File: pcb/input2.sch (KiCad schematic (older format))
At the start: 3 parts, among them U4 PCEngineExpansion

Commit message: Added clock selection
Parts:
- added C68, C78, C80, C81, C84, C85: 10u, custom_components:SM0603_Capa_libcms, symbol pcehd-rescue:C_Small-Device
- added C77, C79: 30p, custom_components:SM0603_Capa_libcms, symbol pcehd-rescue:C_Small-Device
- added C82, C83: 2.2u, custom_components:SM0603_Capa_libcms, symbol pcehd-rescue:C_Small-Device
- added R20, R21: 100k, custom_components:SM0603_Resistor_libcms, symbol ossc_board-rescue:R_Small
- added U14: PCM1862, custom_components:TSSOP-30_4.4x7.8mm_Pitch0.5mm_Handsoldering, symbol ossc_board-rescue:PCM1862
- added Y2: 24.576MHz, custom_components:ECS-3X9X, symbol ossc_board-rescue:Crystal_Small
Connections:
- net labels added: DVDD3V3, I2S_BCK, I2S_DATA, I2S_WS, SCL, SDA, SI_CLK0
- net labels removed: AudioL_O, AudioR_O
- wire segments 17 -> 47
- no-connect marks 10 -> 21

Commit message: Added FS7140 PLL, moved to level-shift '245
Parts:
- removed C77, C79: 30p, custom_components:SM0603_Capa_libcms, symbol pcehd-rescue:C_Small-Device
- removed C78, C80, C81, C84, C85: 10u, custom_components:SM0603_Capa_libcms, symbol pcehd-rescue:C_Small-Device
- removed C82, C83: 2.2u, custom_components:SM0603_Capa_libcms, symbol pcehd-rescue:C_Small-Device
- removed R20, R21: 100k, custom_components:SM0603_Resistor_libcms, symbol ossc_board-rescue:R_Small
- removed U14: PCM1862, custom_components:TSSOP-30_4.4x7.8mm_Pitch0.5mm_Handsoldering, symbol ossc_board-rescue:PCM1862
- removed Y2: 24.576MHz, custom_components:ECS-3X9X, symbol ossc_board-rescue:Crystal_Small
- added C24, C29: 0.1u, custom_components:SM0603_Capa_libcms, symbol pcehd-rescue:C_Small-Device
- added C25, C26, C30: 10u, custom_components:SM0603_Capa_libcms, symbol Device:CP_Small
- added C28, C31, C32, C78, C80: 0.1u, custom_components:SM0603_Capa_libcms, symbol pcehd-rescue:C-Device
- added C77, C79: 1u, custom_components:SM0603_Capa_libcms, symbol Device:CP_Small
- added JP1, JP2, JP3, JP4, JP5, JP6: SolderJumper_2_Open, Jumper:SolderJumper-2_P1.3mm_Open_RoundedPad1.0x1.5mm, symbol Jumper:SolderJumper_2_Open
- added R17, R19: R_Small, custom_components:SM0603_Resistor_libcms, symbol Device:R_Small
- added R20, R21: 10K, custom_components:SM0603_Resistor_libcms, symbol Device:R_Small
- added R6: 4.7k, custom_components:SM0603_Resistor_libcms, symbol pcehd-rescue:R-Device
- added U5: FS7140-01G-XTD, custom_components:FS7140-01G-XTD, symbol custom_components:FS7140-01G-XTD
- added U6: PCM1808PWR, custom_components:PCM1808PWR, symbol custom_components:PCM1808PWR
- added U7: SI5351C-B, custom_components:QFN-20-1EP_4x4mm_Pitch0.5mm_Handsoldering, symbol custom_components:Si5351C
- added U8: 74153, Package_SO:SOIC-16_3.9x9.9mm_P1.27mm, symbol 74xx_IEEE:74153
- added Y1: 25.000MHz, Crystal:Crystal_SMD_SeikoEpson_FA238-4Pin_3.2x2.5mm_HandSoldering, symbol Device:Crystal_GND24_Small
- C68: value 10u -> 0.1u
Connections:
- net labels added: AudioL, AudioR, DCK, DCKFB_I, GNDREF, HSn, IS2_BCK, IS2_DATA, IS2_WS, SI_CLK0_O, SI_CLK1_O, VCCIO
- net labels removed: DVDD3V3, SI_CLK0
- wire segments 47 -> 116
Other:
- moved on the sheet: C27, C68, D4, U4A, U4B

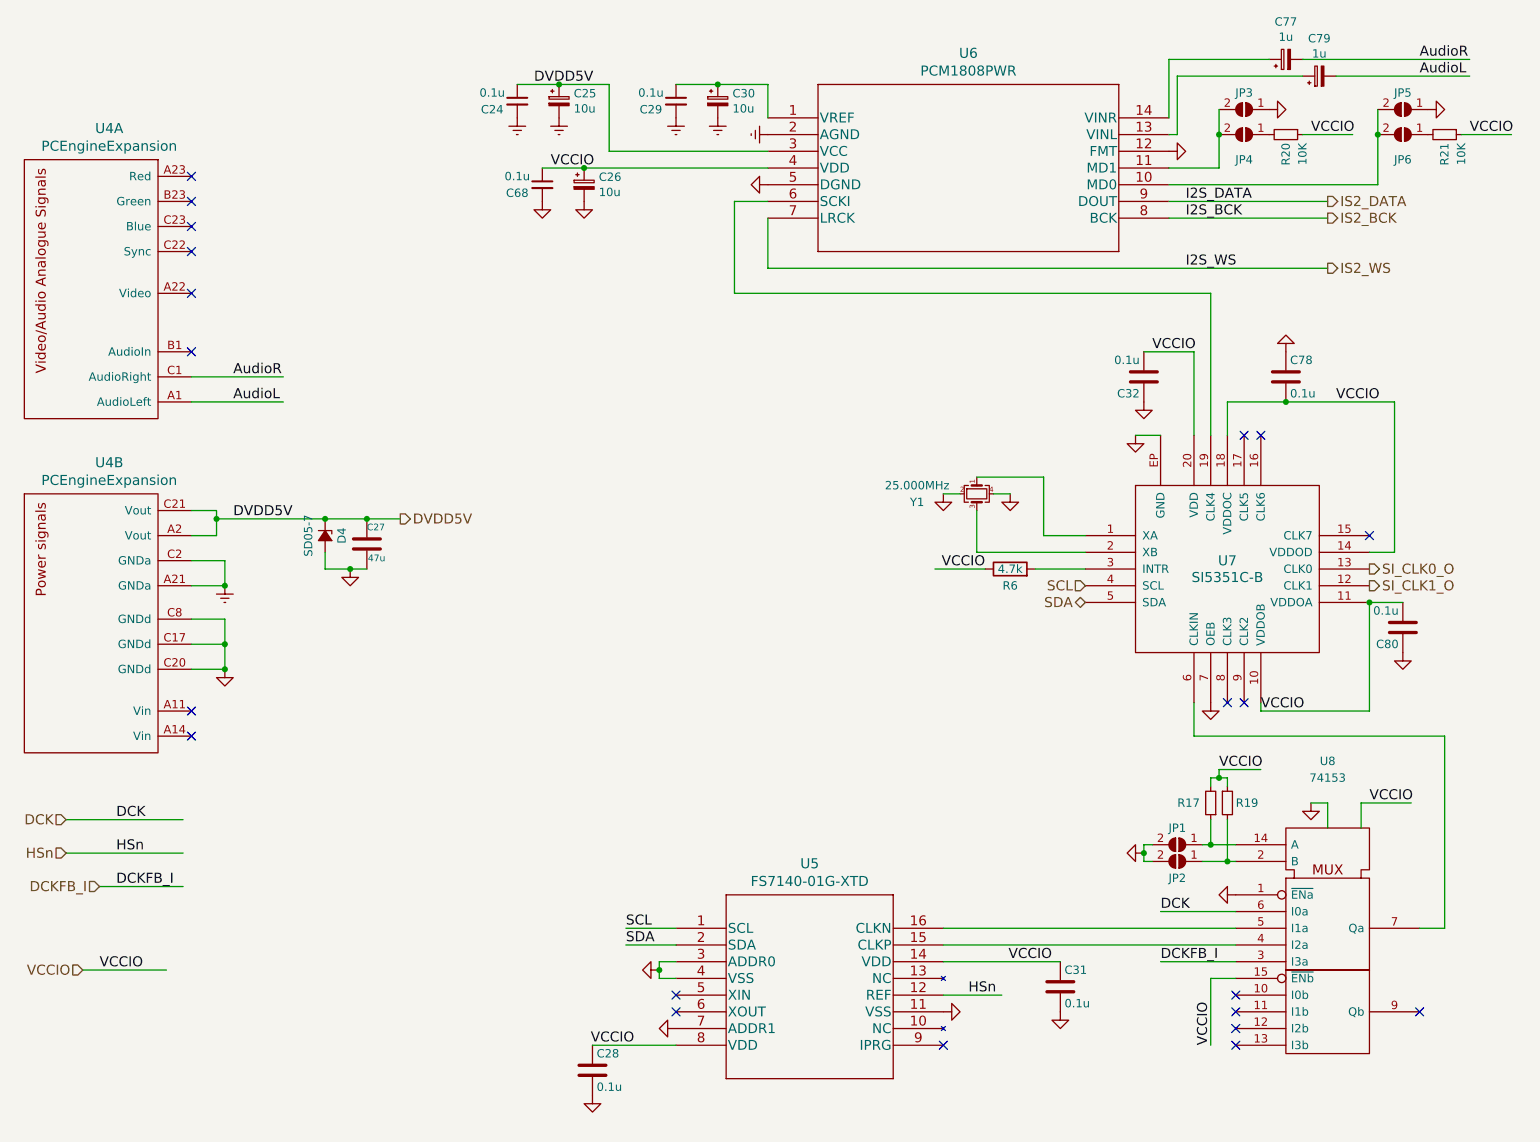
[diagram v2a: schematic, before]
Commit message: Expansion connection re-order for layout
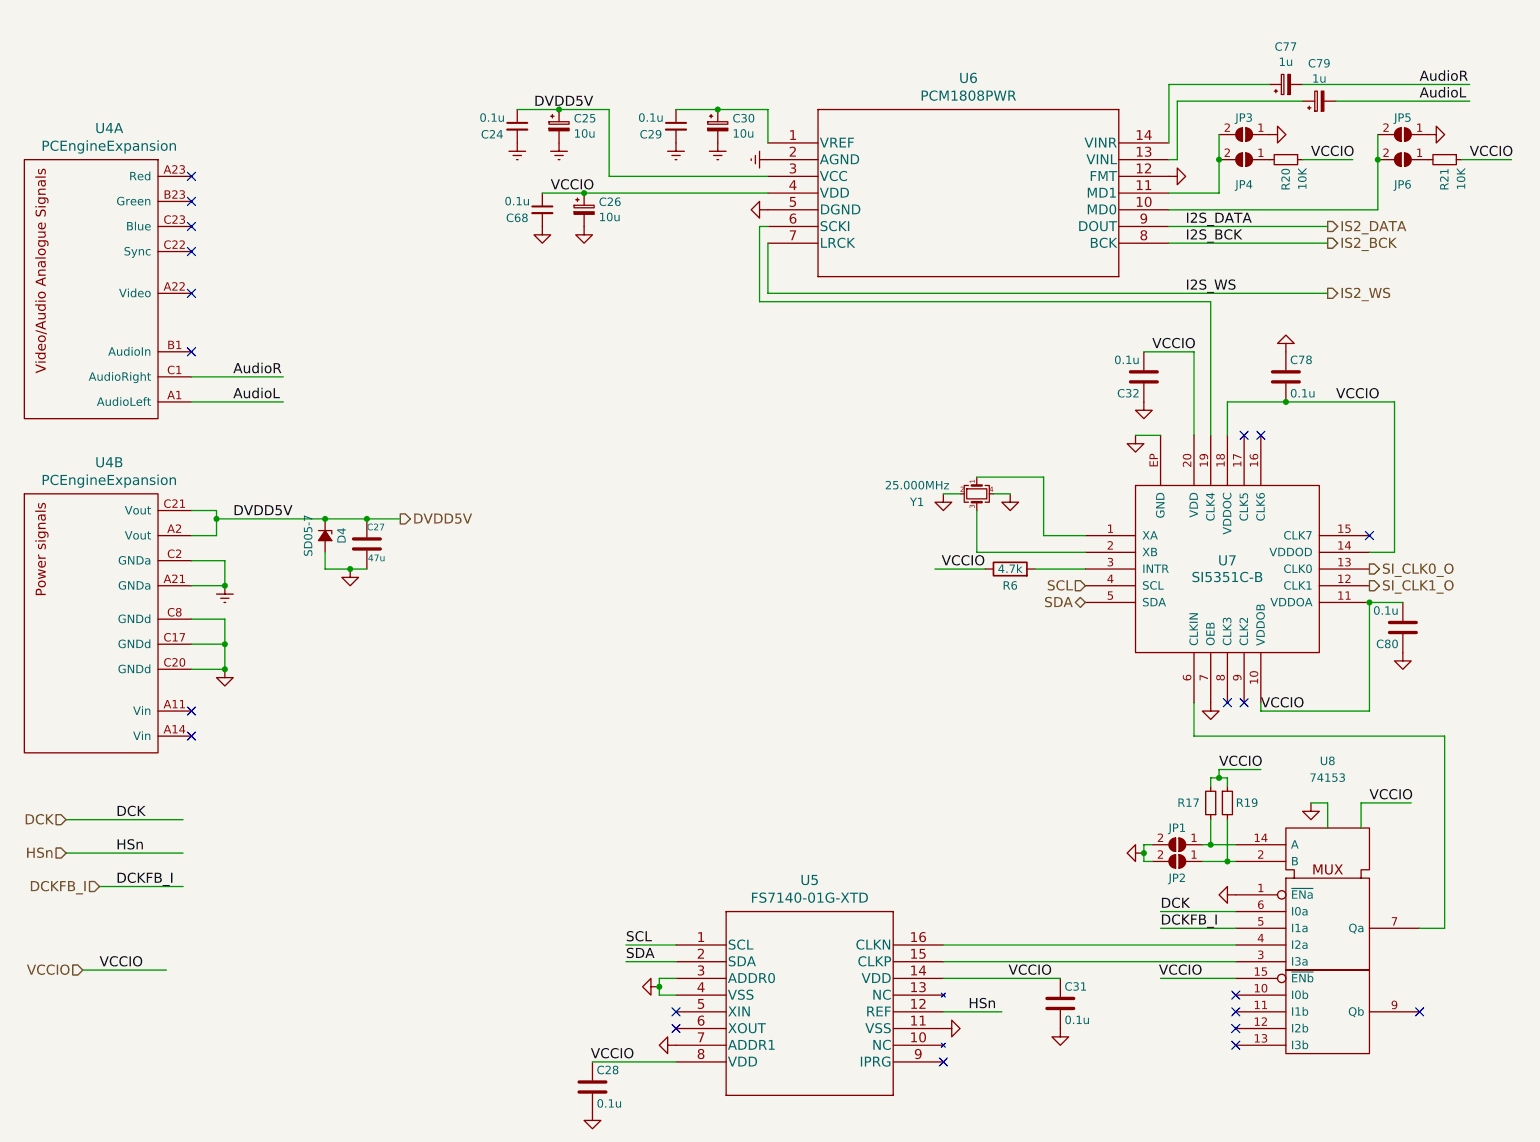
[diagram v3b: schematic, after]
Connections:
- wire segments 116 -> 115
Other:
- moved on the sheet: C24, C25, C26, C28, C29, C30, C31, C68, C77, C79, JP3, JP4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

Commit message: Layout checkpoint
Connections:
- net labels added: HSn_buf
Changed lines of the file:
@@
 HSn
 Text Label 1950 5700 0    60   ~ 0
-HSn
+HSn_buf
 Text Label 1950 5500 0    60   ~ 0
 DCK
@@
 Text Label 5000 6350 0    60   ~ 0
 SDA
-Wire Wire Line
-	6900 6650 7250 6650
-Text Label 7050 6650 0    60   ~ 0
-HSn
+Text Label 7000 6650 0    60   ~ 0
+HSn_buf
 $Comp
 L pcehd-rescue:GND-power #PWR?
@@
 Wire Wire Line
 	5800 2400 5800 1950
+Wire Wire Line
+	6900 6650 7350 6650
 $EndSCHEMATC

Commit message: New layout checkpoint
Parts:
- C25, C26, C30, C77, C79: symbol Device:CP_Small -> pcehd-rescue:CP_Small-Device
- JP1, JP2, JP3, JP4, JP5, JP6: symbol Jumper:SolderJumper_2_Open -> pcehd-rescue:SolderJumper_2_Open-Jumper
- R17, R19, R20, R21: symbol Device:R_Small -> pcehd-rescue:R_Small-Device
- U8: symbol 74xx_IEEE:74153 -> pcehd-rescue:74153-74xx_IEEE
- Y1: symbol Device:Crystal_GND24_Small -> pcehd-rescue:Crystal_GND24_Small-Device
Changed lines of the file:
@@
 EESchema Schematic File Version 4
-LIBS:pcehd-cache
 EELAYER 30 0
 EELAYER END
@@
 	8500 5500 8500 5650
 $Comp
-L Device:R_Small R?
+L pcehd-rescue:R_Small-Device R?
 U 1 1 6105F10D
 P 8500 5400
@@
 $EndComp
 $Comp
-L Device:R_Small R?
+L pcehd-rescue:R_Small-Device R?
 U 1 1 6105F107
 P 8600 5400
@@
 $EndComp
 $Comp
-L Jumper:SolderJumper_2_Open JP?
+L pcehd-rescue:SolderJumper_2_Open-Jumper JP?
 U 1 1 6105F0F4
 P 8300 5750
@@
 $EndComp
 $Comp
-L Jumper:SolderJumper_2_Open JP?
+L pcehd-rescue:SolderJumper_2_Open-Jumper JP?
 U 1 1 6105F0EE
 P 8300 5650
@@
 	7100 3650 7100 3900
 $Comp
-L Device:Crystal_GND24_Small Y?
+L pcehd-rescue:Crystal_GND24_Small-Device Y?
 U 1 1 6105F0AC
 P 7100 3550
@@
 	8650 6050 8200 6050
 $Comp
-L 74xx_IEEE:74153 U?
+L pcehd-rescue:74153-74xx_IEEE U?
 U 1 1 6105F08E
 P 9200 6300
 AR Path="/5A43CDD8/6105F08E" Ref="U?"  Part="1"
 AR Path="/5ECF4034/6105F08E" Ref="U8"  Part="1"
+AR Path="/6105F08E" Ref="U8"  Part="1"
 F 0 "U8" H 9200 7450 50  0000 C CNN
 F 1 "74153" H 9200 7350 50  0000 C CNN
@@
 	2600 3950 2600 4100
 $Comp
-L power:GNDREF #PWR039
+L pcehd-rescue:GNDREF-power #PWR039
 U 1 1 5E270B0A
 P 2600 4100
@@
 Connection ~ 2600 4100
 $Comp
-L power:GNDREF #PWR049
+L pcehd-rescue:GNDREF-power #PWR049
 U 1 1 5E2719D5
 P 5850 1550
@@
 $EndComp
 $Comp
-L power:GNDREF #PWR040
+L pcehd-rescue:GNDREF-power #PWR040
 U 1 1 5E29CC14
 P 4350 1450
@@
 $EndComp
 $Comp
-L power:GNDREF #PWR041
+L pcehd-rescue:GNDREF-power #PWR041
 U 1 1 5E29DCD3
 P 4600 1450
@@
 $EndComp
 $Comp
-L power:GNDREF #PWR045
+L pcehd-rescue:GNDREF-power #PWR045
 U 1 1 5E2A9BFC
 P 5300 1450
@@
 $EndComp
 $Comp
-L power:GNDREF #PWR048
+L pcehd-rescue:GNDREF-power #PWR048
 U 1 1 5E2A9C02
 P 5550 1450
@@
 	4500 1750 4750 1750
 $Comp
-L Device:CP_Small C25
+L pcehd-rescue:CP_Small-Device C25
 U 1 1 5E2BC07C
 P 4600 1350
@@
 	4600 1250 4900 1250
 $Comp
-L Device:CP_Small C26
+L pcehd-rescue:CP_Small-Device C26
 U 1 1 5E2BC749
 P 4750 1850
@@
 	5300 1250 5550 1250
 $Comp
-L Device:CP_Small C30
+L pcehd-rescue:CP_Small-Device C30
 U 1 1 5E2BCBD4
 P 5550 1350
@@
 	8300 1550 8250 1550
 $Comp
-L Device:CP_Small C79
+L pcehd-rescue:CP_Small-Device C79
 U 1 1 5E2BD348
 P 9150 1200
@@
 	8250 1450 8250 1100
 $Comp
-L Device:CP_Small C77
+L pcehd-rescue:CP_Small-Device C77
 U 1 1 5E2BB078
 P 8950 1100
@@
 	8250 1100 8850 1100
 $Comp
-L Jumper:SolderJumper_2_Open JP?
+L pcehd-rescue:SolderJumper_2_Open-Jumper JP?
 U 1 1 5E309383
 P 8700 1400
@@
 $EndComp
 $Comp
-L Jumper:SolderJumper_2_Open JP?
+L pcehd-rescue:SolderJumper_2_Open-Jumper JP?
 U 1 1 5E309389
 P 8700 1550
@@
 	8550 1550 8550 1400
 $Comp
-L Jumper:SolderJumper_2_Open JP?
+L pcehd-rescue:SolderJumper_2_Open-Jumper JP?
 U 1 1 5E30DFC8
 P 9650 1400
@@
 $EndComp
 $Comp
-L Jumper:SolderJumper_2_Open JP?
+L pcehd-rescue:SolderJumper_2_Open-Jumper JP?
 U 1 1 5E30DFCE
 P 9650 1550
@@
 	9500 1550 9500 1850
 $Comp
-L Device:R_Small R?
+L pcehd-rescue:R_Small-Device R?
 U 1 1 5E334741
 P 8950 1550
@@
 $EndComp
 $Comp
-L Device:R_Small R?
+L pcehd-rescue:R_Small-Device R?
 U 1 1 5E33651E
 P 9900 1550

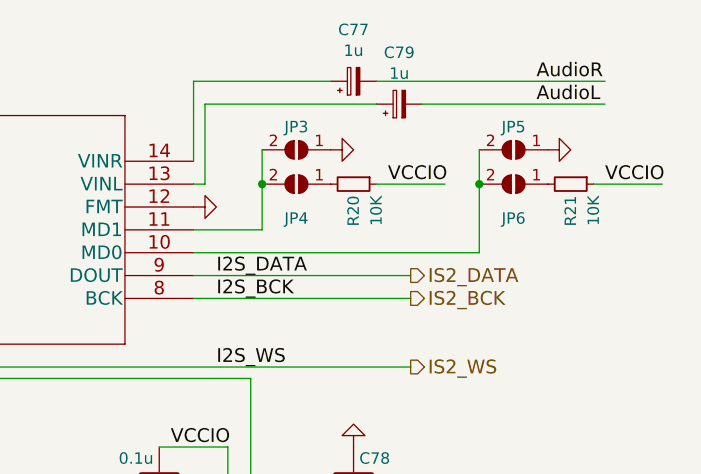
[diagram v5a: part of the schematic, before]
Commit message: Removed unneeded jumpers
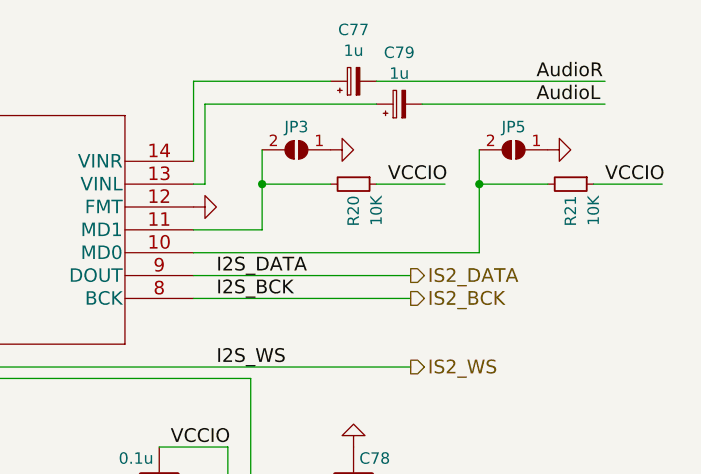
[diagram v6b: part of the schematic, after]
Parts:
- removed JP4, JP6: SolderJumper_2_Open, Jumper:SolderJumper-2_P1.3mm_Open_RoundedPad1.0x1.5mm, symbol pcehd-rescue:SolderJumper_2_Open-Jumper
- R17, R19: value R_Small -> 10K
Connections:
- wire segments 115 -> 117
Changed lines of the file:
@@
 EESchema Schematic File Version 4
+LIBS:pcehd-cache
 EELAYER 30 0
 EELAYER END
@@
 Sheet 4 5
 Title "PCEHD"
-Date "2020-01-12"
+Date "2020-01-16"
 Rev "0.1"
 Comp ""
@@
 AR Path="/5ECF4034/6105F10D" Ref="R17"  Part="1"
 F 0 "R17" H 8700 5400 50  0000 R CNN
-F 1 "R_Small" H 8850 5450 50  0001 R CNN
+F 1 "10K" H 8850 5450 50  0001 R CNN
 F 2 "custom_components:SM0603_Resistor_libcms" H 8500 5400 50  0001 C CNN
 F 3 "~" H 8500 5400 50  0001 C CNN
@@
 AR Path="/5ECF4034/6105F107" Ref="R19"  Part="1"
 F 0 "R19" H 8650 5400 50  0000 L CNN
-F 1 "R_Small" H 8659 5355 50  0001 L CNN
+F 1 "10K" H 8659 5355 50  0001 L CNN
 F 2 "custom_components:SM0603_Resistor_libcms" H 8600 5400 50  0001 C CNN
 F 3 "~" H 8600 5400 50  0001 C CNN
@@
 $Comp
 L pcehd-rescue:SolderJumper_2_Open-Jumper JP?
-U 1 1 5E309389
-P 8700 1550
-AR Path="/5A43CDD8/5E309389" Ref="JP?"  Part="1"
-AR Path="/5ECF4034/5E309389" Ref="JP4"  Part="1"
-F 0 "JP4" H 8700 1700 50  0000 C CNN
-F 1 "SolderJumper_2_Open" H 8700 1664 50  0001 C CNN
-F 2 "Jumper:SolderJumper-2_P1.3mm_Open_RoundedPad1.0x1.5mm" H 8700 1550 50  0001 C CNN
-F 3 "~" H 8700 1550 50  0001 C CNN
-	1    8700 1550
-	-1   0    0    1
-$EndComp
-Connection ~ 8550 1550
-Wire Wire Line
-	8550 1550 8550 1400
-$Comp
-L pcehd-rescue:SolderJumper_2_Open-Jumper JP?
 U 1 1 5E30DFC8
 P 9650 1400
@@
 	-1   0    0    1
 $EndComp
-$Comp
-L pcehd-rescue:SolderJumper_2_Open-Jumper JP?
-U 1 1 5E30DFCE
-P 9650 1550
-AR Path="/5A43CDD8/5E30DFCE" Ref="JP?"  Part="1"
-AR Path="/5ECF4034/5E30DFCE" Ref="JP6"  Part="1"
-F 0 "JP6" H 9650 1700 50  0000 C CNN
-F 1 "SolderJumper_2_Open" H 9650 1664 50  0001 C CNN
-F 2 "Jumper:SolderJumper-2_P1.3mm_Open_RoundedPad1.0x1.5mm" H 9650 1550 50  0001 C CNN
-F 3 "~" H 9650 1550 50  0001 C CNN
-	1    9650 1550
-	-1   0    0    1
-$EndComp
-Connection ~ 9500 1550
-Wire Wire Line
-	9500 1550 9500 1400
 Wire Wire Line
 	8250 1750 8550 1750
 Wire Wire Line
-	8550 1550 8550 1750
-Wire Wire Line
 	8250 1850 9500 1850
-Wire Wire Line
-	9500 1550 9500 1850
 $Comp
 L pcehd-rescue:R_Small-Device R?
@@
 Wire Wire Line
 	6900 6650 7350 6650
+Wire Wire Line
+	8550 1400 8550 1550
+Wire Wire Line
+	9500 1400 9500 1550
+Wire Wire Line
+	8850 1550 8550 1550
+Connection ~ 8550 1550
+Wire Wire Line
+	8550 1550 8550 1750
+Wire Wire Line
+	9800 1550 9500 1550
+Connection ~ 9500 1550
+Wire Wire Line
+	9500 1550 9500 1850
 $EndSCHEMATC

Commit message: Layout checkpoint
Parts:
- added C93: 0.1u, custom_components:SM0603_Capa_libcms, symbol pcehd-rescue:C-Device
- added C94, C95: 47u, custom_components:SM0603_Capa_libcms, symbol pcehd-rescue:C-Device
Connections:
- wire segments 117 -> 122
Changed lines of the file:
@@
 $EndComp
-Wire Wire Line
-	3350 4000 3450 4000
 Wire Wire Line
 	3450 3700 3650 3700
 Wire Wire Line
 	3200 3700 3450 3700
-Text HLabel 3650 3700 2    60   Output ~ 0
+Text HLabel 4150 3700 2    60   Output ~ 0
 DVDD5V
-Connection ~ 3350 4000
 Connection ~ 3450 3700
 Connection ~ 3200 3700
 Wire Wire Line
-	3200 4000 3350 4000
-Wire Wire Line
 	3200 3900 3200 4000
 $Comp
 L pcehd-rescue:GND-power #PWR?
 U 1 1 5ED1A2B6
-P 3350 4000
+P 3550 4100
 AR Path="/5A43CDD8/5ED1A2B6" Ref="#PWR?"  Part="1"
 AR Path="/5ECF4034/5ED1A2B6" Ref="#PWR052"  Part="1"
-F 0 "#PWR052" H 3350 4000 30  0001 C CNN
-F 1 "GND" H 3350 3930 30  0001 C CNN
-F 2 "" H 3350 4000 60  0001 C CNN
-F 3 "" H 3350 4000 60  0000 C CNN
-	1    3350 4000
+F 0 "#PWR052" H 3550 4100 30  0001 C CNN
+F 1 "GND" H 3550 4030 30  0001 C CNN
+F 2 "" H 3550 4100 60  0001 C CNN
+F 3 "" H 3550 4100 60  0000 C CNN
+	1    3550 4100
 	1    0    0    -1
 $EndComp
@@
 Wire Wire Line
 	9500 1550 9500 1850
+$Comp
+L pcehd-rescue:C-Device C?
+U 1 1 5E2436B3
+P 9700 5550
+AR Path="/5A43CDD8/5E2436B3" Ref="C?"  Part="1"
+AR Path="/5ECF4034/5E2436B3" Ref="C93"  Part="1"
+F 0 "C93" H 9725 5650 50  0000 L CNN
+F 1 "0.1u" H 9725 5450 50  0000 L CNN
+F 2 "custom_components:SM0603_Capa_libcms" H 9738 5400 50  0001 C CNN
+F 3 "" H 9700 5550 50  0000 C CNN
+	1    9700 5550
+	1    0    0    -1
+$EndComp
+$Comp
+L pcehd-rescue:GND-power #PWR?
+U 1 1 5E2445FC
+P 9700 5700
+AR Path="/5A43CDD8/5E2445FC" Ref="#PWR?"  Part="1"
+AR Path="/5ECF4034/5E2445FC" Ref="#PWR0179"  Part="1"
+F 0 "#PWR0179" H 9700 5700 30  0001 C CNN
+F 1 "GND" H 9700 5630 30  0001 C CNN
+F 2 "" H 9700 5700 60  0001 C CNN
+F 3 "" H 9700 5700 60  0000 C CNN
+	1    9700 5700
+	1    0    0    -1
+$EndComp
+$Comp
+L pcehd-rescue:C-Device C?
+U 1 1 5E24D671
+P 3650 3850
+AR Path="/5A43CDD8/5E24D671" Ref="C?"  Part="1"
+AR Path="/5ECF4034/5E24D671" Ref="C94"  Part="1"
+F 0 "C94" H 3650 3950 40  0000 L CNN
+F 1 "47u" H 3656 3765 40  0000 L CNN
+F 2 "custom_components:SM0603_Capa_libcms" H 3688 3700 30  0001 C CNN
+F 3 "~" H 3650 3850 60  0000 C CNN
+	1    3650 3850
+	1    0    0    -1
+$EndComp
+$Comp
+L pcehd-rescue:C-Device C?
+U 1 1 5E251A93
+P 3850 3850
+AR Path="/5A43CDD8/5E251A93" Ref="C?"  Part="1"
+AR Path="/5ECF4034/5E251A93" Ref="C95"  Part="1"
+F 0 "C95" H 3850 3950 40  0000 L CNN
+F 1 "47u" H 3856 3765 40  0000 L CNN
+F 2 "custom_components:SM0603_Capa_libcms" H 3888 3700 30  0001 C CNN
+F 3 "~" H 3850 3850 60  0000 C CNN
+	1    3850 3850
+	1    0    0    -1
+$EndComp
+Wire Wire Line
+	3650 3700 3850 3700
+Connection ~ 3650 3700
+Wire Wire Line
+	3450 4000 3550 4000
+Wire Wire Line
+	3650 4000 3850 4000
+Connection ~ 3450 4000
+Connection ~ 3650 4000
+Wire Wire Line
+	3200 4000 3450 4000
+Wire Wire Line
+	3550 4000 3550 4100
+Connection ~ 3550 4000
+Wire Wire Line
+	3550 4000 3650 4000
+Wire Wire Line
+	3850 3700 4150 3700
+Connection ~ 3850 3700
 $EndSCHEMATC
